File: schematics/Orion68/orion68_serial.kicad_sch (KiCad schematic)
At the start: 32 parts, among them J700 Euro96pin, J701 RS232_1, J702 RS232_1, J703 RS232_1, U18_C? 100nf, U20 74HC138, U701 UART1, U702 UART2, U703 UART3, Y1 14.745600

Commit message: Implementation drive ide initiated
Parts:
- removed J700: Euro96pin, ConnPdSilva:conn_euro96, symbol ConnPdSilva:ConnEuro96
- added C9: 1000uF, symbol Device:C_Polarized
- added D7: LED, symbol Device:LED
- added J11: IDE-40W, symbol Connector_Generic:Conn_02x20_Odd_Even
- added J12: PWR, symbol Connector_Generic:Conn_02x01
- added R19, R20, R21, R22, R27, R28, R33, R34, R43, R44, R45, R46, R47, R48, R49, R52: 33R, symbol Device:R
- added R35, R36, R37, R38, R39, R40, R41, R42: 27R, symbol Device:R
- added R50, R51: 2k2, symbol Device:R
- added U17, U19: 74LS139, symbol 74xx:74LS139
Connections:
- net BD0: now also R43.1; no longer U700.66 (D0)
- net BD1: now also R44.1; no longer U700.67 (D1)
- net BD2: now also R45.1; no longer U700.68 (D2)
- net BD3: now also R46.1; no longer U700.1 (D3)
- net BD4: now also R47.1; no longer U700.2 (D4)
- net BD5: now also R48.1; no longer U700.3 (D5)
- net BD6: now also R49.1; no longer U700.4 (D6)
- net BD7: now also R52.1; no longer U700.5 (D7)
- net GND: now also C9.2, J11.19 (Pin_19), J11.2 (Pin_2), J11.22 (Pin_22), J11.24 (Pin_24), J11.26 (Pin_26), J11.28 (Pin_28), J11.30 (Pin_30), J11.40 (Pin_40), U19.3 (A1)
- net /RESET: now also J11.1 (Pin_1)
- net /memrd: now also J700.73
- net /memwr: now also J700.74, U19.2 (A0)
- net /CS_IDE_ATA: now reaches U20.11 (~{Y4})
- net /CS_IDE_ATA: now also J11.37 (Pin_37), U19.1 (E)
- new net: D7.1 (K), R51.2
- new net: J11.20 (Pin_20), J12.1 (Pin_1)
- new net: R44.2, U700.67 (D1)
- new net: J11.39 (Pin_39), R51.1
- new net: R52.2, U700.5 (D7)
- new net: J11.38 (Pin_38), R50.1
- new net: R46.2, U700.1 (D3)
- new net: R47.2, U700.2 (D4)
- new net: R48.2, U700.3 (D5)
- new net: R49.2, U700.4 (D6)
- new net: R43.2, U700.66 (D0)
- new net: R45.2, U700.68 (D2)
- new net 5V: C9.1, D7.2 (A), J12.2 (Pin_2), R50.2
- new net A1: J11.35 (Pin_35)
- new net A2: J11.33 (Pin_33)
- new net A3: J11.36 (Pin_36)
- new net P_D0: J11.17 (Pin_17), R34.2, R42.1
- new net P_D1: J11.15 (Pin_15), R33.2, R41.1
- new net P_D10: J11.8 (Pin_8), R28.1, R40.2
- new net P_D11: J11.10 (Pin_10), R27.1, R39.2
- new net P_D12: J11.12 (Pin_12), R22.1, R38.2
- new net P_D13: J11.14 (Pin_14), R21.1, R37.2
- new net P_D14: J11.16 (Pin_16), R20.1, R36.2
- new net P_D15: J11.18 (Pin_18), R19.1, R35.2
- new net P_D2: J11.13 (Pin_13), R28.2, R40.1
- new net P_D3: J11.11 (Pin_11), R27.2, R39.1
- new net P_D4: J11.9 (Pin_9), R22.2, R38.1
- new net P_D5: J11.7 (Pin_7), R21.2, R37.1
- new net P_D6: J11.5 (Pin_5), R20.2, R36.1
- new net P_D7: J11.3 (Pin_3), R19.2, R35.1
- new net P_D8: J11.4 (Pin_4), R34.1, R42.2
- new net P_D9: J11.6 (Pin_6), R33.1, R41.2
- new net /RD: J11.25 (Pin_25), U19.5 (O1)
- new net /WR: J11.23 (Pin_23), U19.4 (O0)
- no-connect marks 20 -> 25
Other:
- note added: "FF4000 - FF40FF UART0 FF4100 - FF41FF UART1 FF4200 - FF42FF UART2 FF4300 - FF43FF UART3 FF4400 - FF44FF Hard disk ATA/IDE"
- note removed: "15 14 13 12 11 10"
- note removed: "FF4000 – FF40FF UART0 FF4100 – FF91FF UART1 FF4200 - FF92FF UART2 FF4300 - FF93FF UART3"
- moved on the sheet: C4, C5, J700, R23, R24, U18_C?, U700, Y1

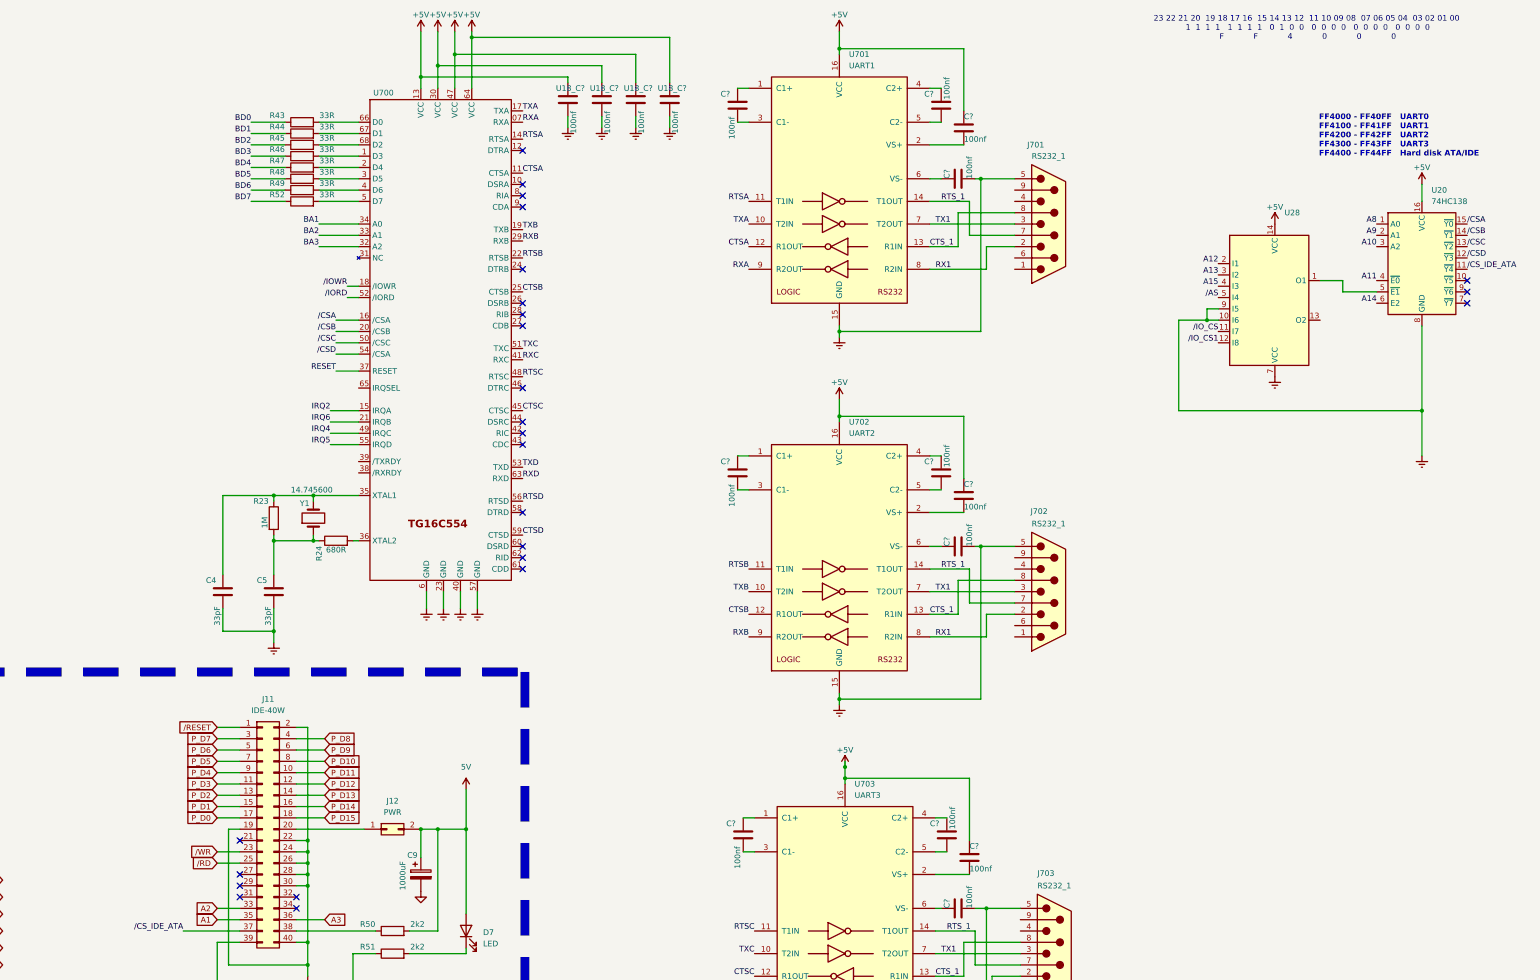
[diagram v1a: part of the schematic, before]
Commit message: Version 1.2 picoVGA implemented a workaround for the UART issue
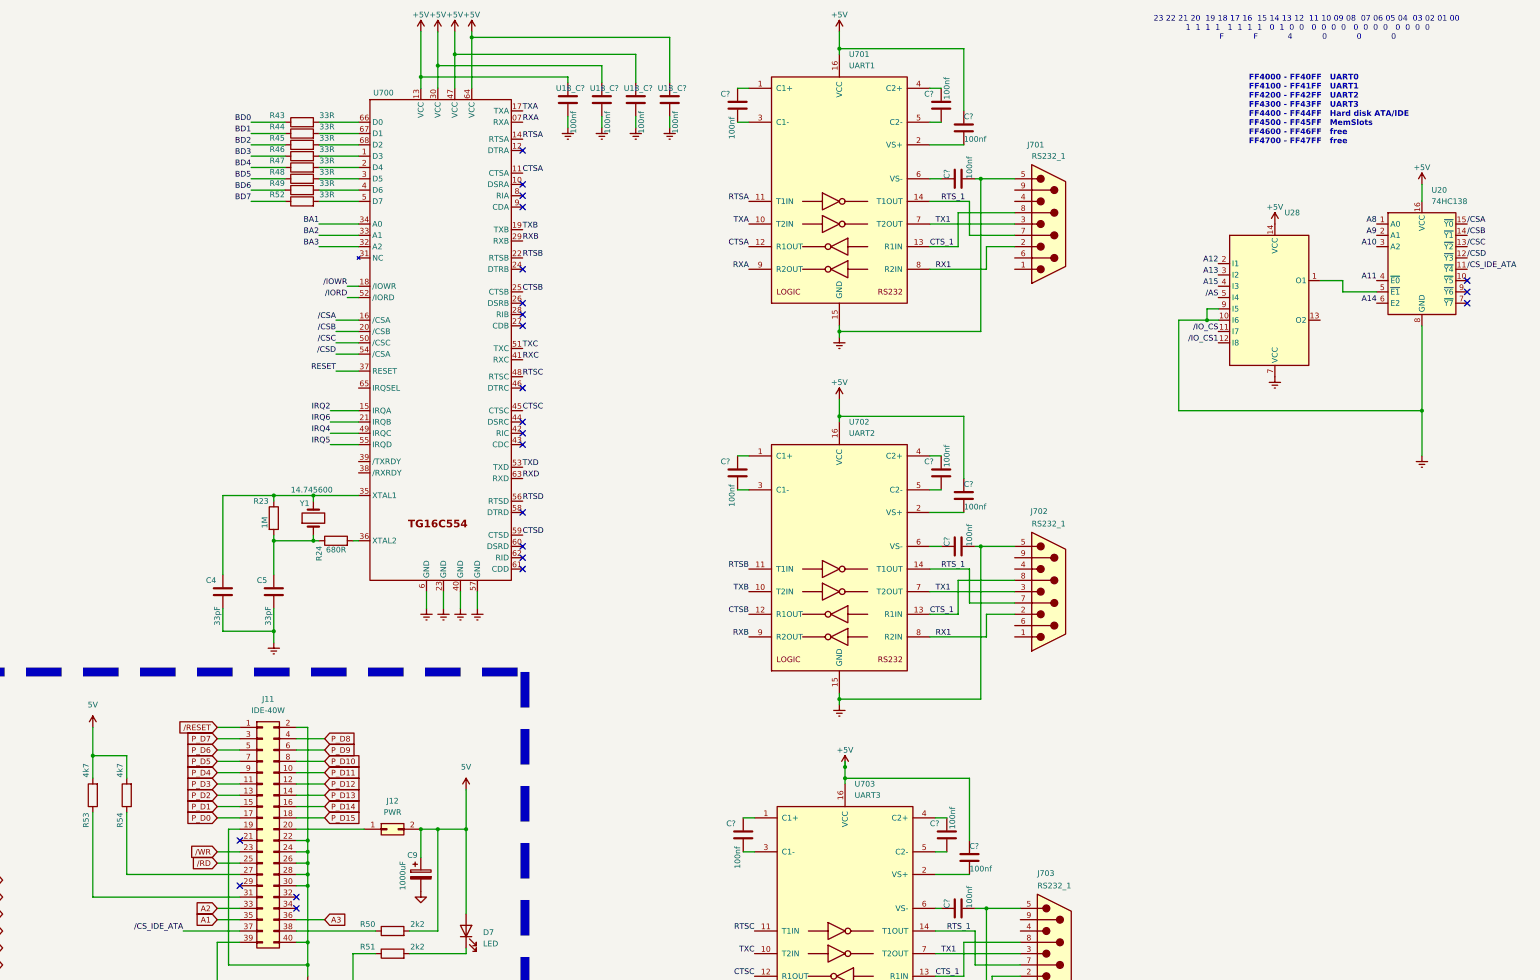
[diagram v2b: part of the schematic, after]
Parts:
- added R53, R54: 4k7, symbol Device:R
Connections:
- net 5V: now also R53.2, R54.2
- net at J11.27 (Pin_27): now also R54.1
- net at J11.31 (Pin_31): now also R53.1
- no-connect marks 25 -> 23
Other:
- note added: "FF4000 - FF40FF UART0 FF4100 - FF41FF UART1 FF4200 - FF42FF UART2 FF4300 - FF43FF UART3 FF4400 - FF44FF Hard disk ATA/IDE FF4500 - FF45FF MemSlots FF4600 - FF46FF free FF4700 - FF47FF free"
- note removed: "FF4000 - FF40FF UART0 FF4100 - FF41FF UART1 FF4200 - FF42FF UART2 FF4300 - FF43FF UART3 FF4400 - FF44FF Hard disk ATA/IDE"
